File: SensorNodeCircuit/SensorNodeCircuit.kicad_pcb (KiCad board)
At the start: 2 copper layers, 71.6 x 36.1 mm, 26 parts, among them J1 USB_B_Micro, J2 FTDI, J3 ExtraPins, J4 ProgJump, J5 PWR, J6 MuxExtra, SW1 ResetButton, U1 AMS1117-3.3, U2 ESP-12F, U3 CD4051B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

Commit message: Finished sensor node pcb layout
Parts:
- moved J5 12.9 mm to (107.7, 80.3), turned to 0 degrees
- moved J6 12.5 mm to (117.3, 83.3), turned to 180 degrees
- moved R9 1.80 mm to (126.5, 81.4)
- moved U1 1.61 mm to (115.3, 93.0)
- moved C1 1.61 mm to (113.5, 98.5)
- moved C2 1.61 mm to (113.5, 101.0)
- moved J3 1.56 mm to (146.0, 107.5)
- moved U2 1.02 mm to (156.5, 90.3)
- moved R1 1.02 mm to (153.1, 88.1)
- moved R2 1.02 mm to (153.1, 90.6)
- moved R3 1.02 mm to (153.1, 93.3)
- moved R4 1.02 mm to (159.7, 99.0)
- moved R5 1.02 mm to (159.7, 96.6)
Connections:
- J2 pad 4: +3.3V -> +3V3
- J3 pad 1: SDA -> SCL
- J3 pad 2: SCL -> SDA
- J5 pad 2: +3.3V -> +3V3
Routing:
- net GND: track 0.00 -> 253.2 mm
- net +3V3: track 0.00 -> 120.3 mm, vias 0 -> 1
- net +5V: track 0.00 -> 57.5 mm
- net DHTOut: track 0.00 -> 33.3 mm
- net SCL: track 0.00 -> 30.2 mm, vias 0 -> 2
- net SDA: track 0.00 -> 26.0 mm, vias 0 -> 2
- net MuxB: track 0.00 -> 24.2 mm, vias 0 -> 1
- net RST: track 0.00 -> 23.6 mm
- net MuxA: track 0.00 -> 23.0 mm, vias 0 -> 1
- net SensorC: track 0.00 -> 22.9 mm
- net TempOut: track 0.00 -> 22.3 mm
- net ADC: track 0.00 -> 21.5 mm, vias 0 -> 3
- net LDROut: track 0.00 -> 18.8 mm, vias 0 -> 1
- net SensorD: track 0.00 -> 18.1 mm
- net +3.3V: track 0.00 -> 14.9 mm
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- added copper zone on B.Cu, net GND
- added copper zone on F.Cu, net GND
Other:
- board text added: "+"
- board text added: "+3V3"
- board text added: "+5V"
- board text added: "-"
- board text added: "G"
- board text added: "GND"
- board text added: "MuxC"
- board text added: "MuxD"
- board text added: "Reset"
- board text added: "Rx"
- board text added: "Tx"

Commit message: Generated gerbers
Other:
- board text added: "Boot"
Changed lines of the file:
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@@
   (general
     (thickness 1.6)
-    (drawings 18)
+    (drawings 19)
     (tracks 274)
     (zones 0)
@@
     (visible_elements FFFFFF7F)
     (pcbplotparams
-      (layerselection 0x010fc_ffffffff)
+      (layerselection 0x010f0_ffffffff)
       (usegerberextensions false)
       (usegerberattributes false)
@@
       (viasonmask false)
       (mode 1)
-      (useauxorigin false)
+      (useauxorigin true)
       (hpglpennumber 1)
       (hpglpenspeed 20)
@@
       (outputformat 1)
       (mirror false)
-      (drillshape 1)
+      (drillshape 0)
       (scaleselection 1)
       (outputdirectory ""))
@@
     )
   )
+  (gr_text Boot (at 169.418 103.886) (layer F.SilkS)
+    (effects (font (size 1 1) (thickness 0.15)))
+  )
   (gr_text MuxD (at 121.158 83.4136) (layer F.SilkS)

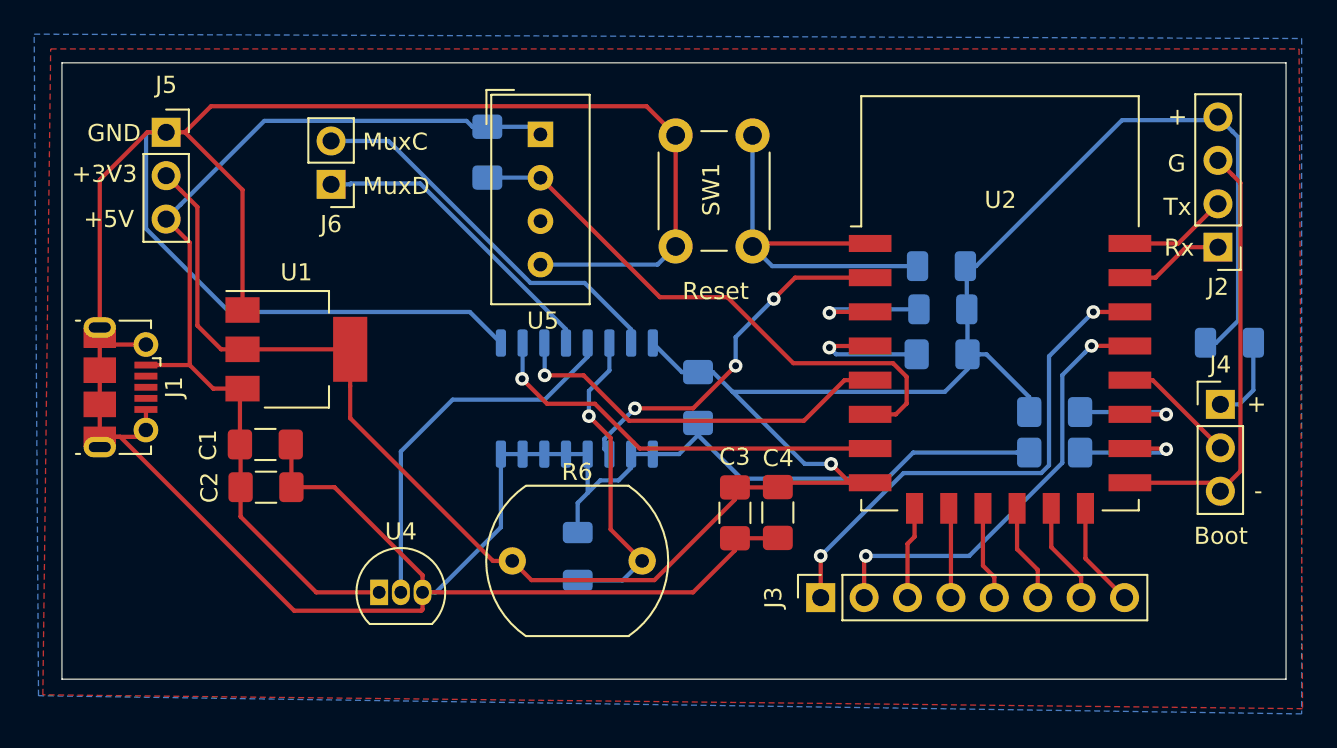
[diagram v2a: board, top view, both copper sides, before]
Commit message: Added sensor circuit v2
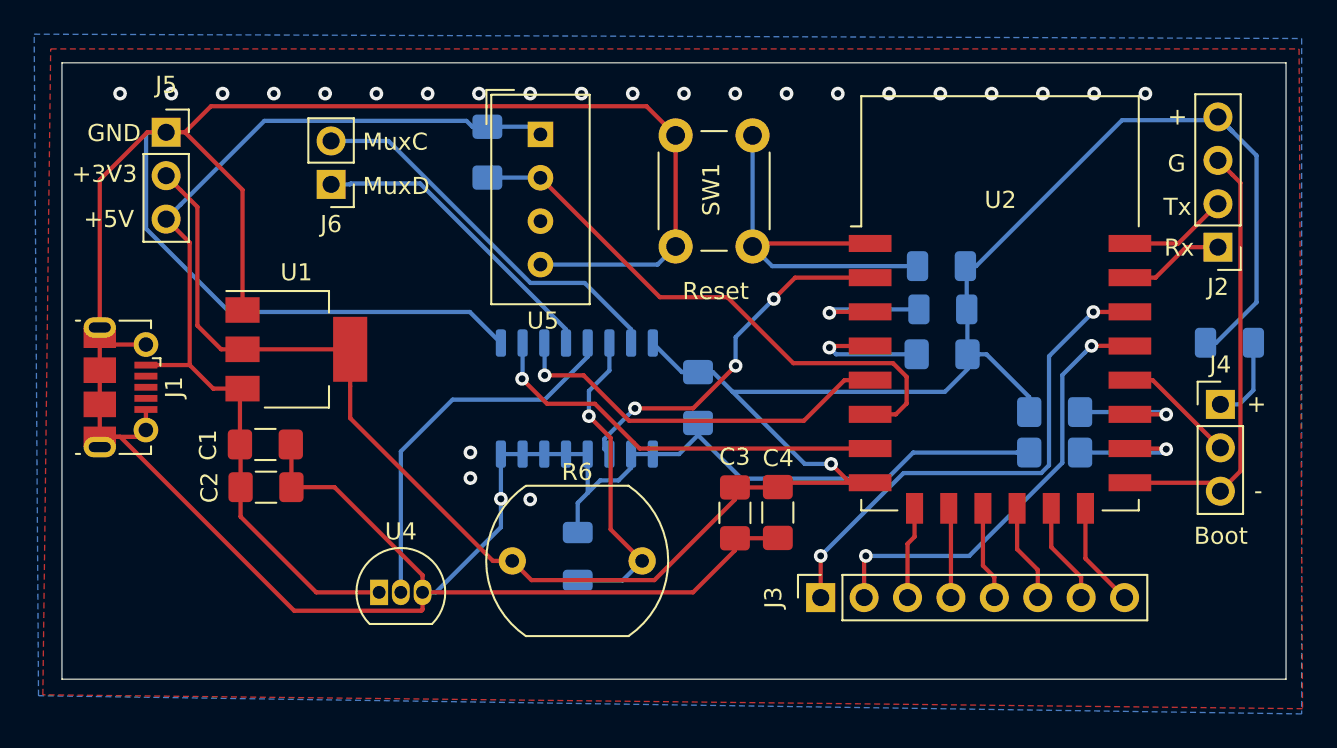
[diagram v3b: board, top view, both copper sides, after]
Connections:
- R8 pad 1: +3.3V -> +3V3
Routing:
- net +3V3: track 120.3 -> 137.2 mm
- net +3.3V: track 14.9 -> 0.00 mm
- net GND: vias 0 -> 25

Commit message: Sensor node pcb updated
Added voltage divider to temp sensor output, and thicker power traces
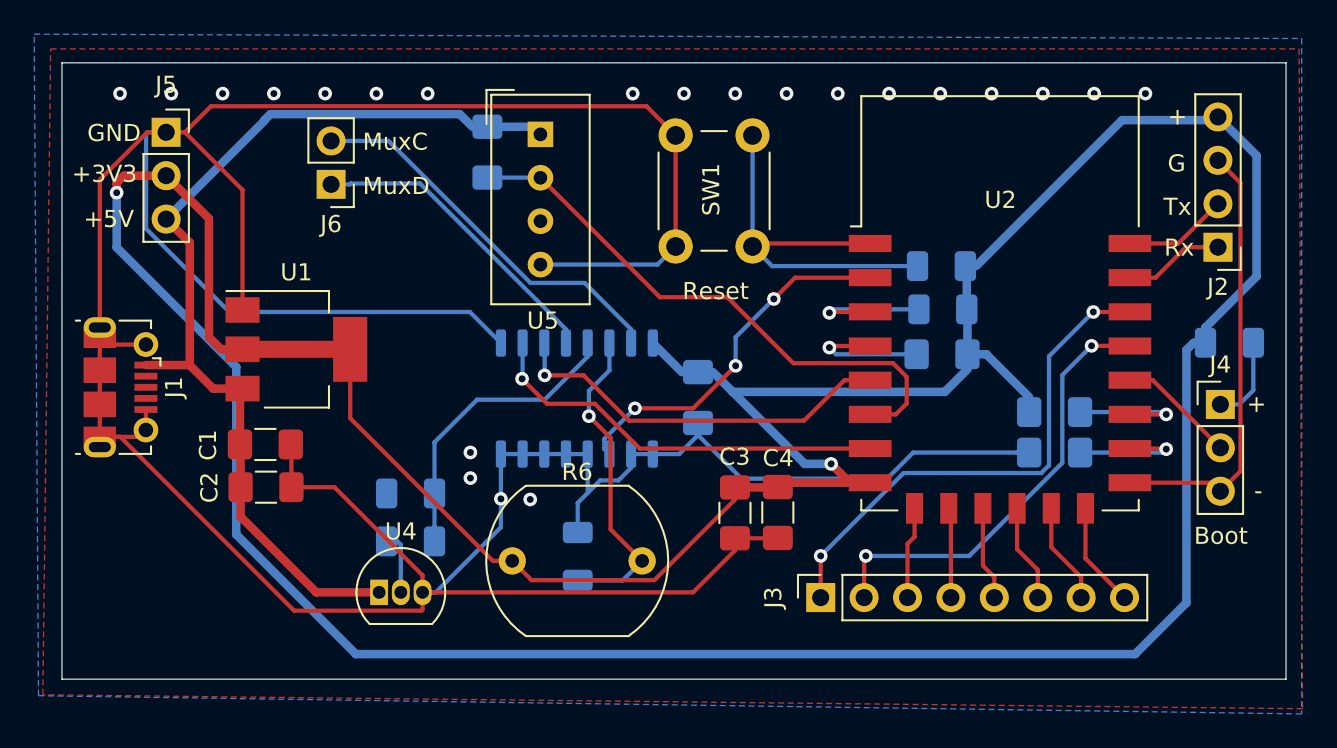
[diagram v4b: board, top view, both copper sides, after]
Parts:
- added R10: 10k, Resistor_SMD:R_1206_3216Metric, B.Cu at (122.0, 104.2)
- added R11: 20k, Resistor_SMD:R_1206_3216Metric, B.Cu at (122.0, 101.4)
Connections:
- U4 pad 2: TempOut -> Net-(R10-Pad2)
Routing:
- net +3V3: track 137.2 -> 239.8 mm, vias 1 -> 2
- net TempOut: track 22.3 -> 17.6 mm
- net Net-(R10-Pad2): track 0.00 -> 3.70 mm
- net GND: vias 25 -> 22
